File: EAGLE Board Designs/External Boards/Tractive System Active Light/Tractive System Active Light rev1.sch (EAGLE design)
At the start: 26 parts, among them X1 CONNECTOR-4NANO-FIT-VERTICAL-4

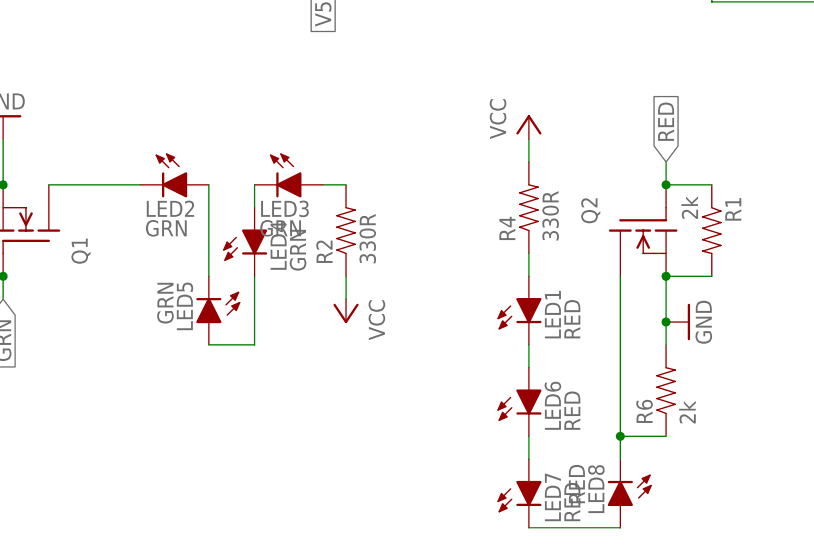
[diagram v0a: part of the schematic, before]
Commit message: Fixed thermal pads to have seperate net
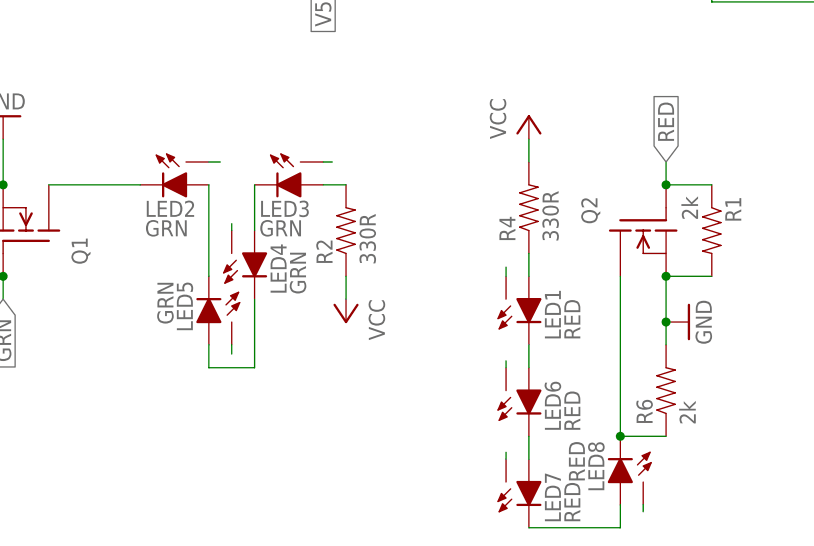
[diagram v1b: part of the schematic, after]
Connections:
- new net LED1_THERM: LED1.X
- new net LED2_THERM: LED2.X
- new net LED3_THERM: LED3.X
- new net LED4_THERM: LED4.X
- new net LED5_THERM: LED5.X
- new net LED6_THERM: LED6.X
- new net LED7_THERM: LED7.X
- new net LED8_THERM: LED8.X
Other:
- moved on the sheet: LED4, LED8
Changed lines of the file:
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@@
 <part name="Q1" library="HyTechDevices" deviceset="DMG3406L" device="SOT"/>
 <part name="Q2" library="HyTechDevices" deviceset="DMG3406L" device="SOT"/>
-<part name="NA555" library="HyTechDevices" deviceset="NA555" device="SO-8" package3d_urn="urn:adsk.eagle:package:30987/2"/>
+<part name="NA555" library="HyTechDevices" deviceset="NA555" device="SO-8"/>
 <part name="LED1" library="HyTechDevices" deviceset="XP-E2" device="XP-E2" value="RED"/>
 <part name="LED2" library="HyTechDevices" deviceset="XP-E2" device="XP-E2" value="GRN"/>
@@
 <attribute name="VALUE" x="3.048" y="32.385" size="1.778" layer="96"/>
 </instance>
-<instance part="LED4" gate="G$1" x="2.54" y="33.02" smashed="yes">
-<attribute name="NAME" x="6.096" y="28.448" size="1.778" layer="95" rot="R90"/>
-<attribute name="VALUE" x="8.255" y="28.448" size="1.778" layer="96" rot="R90"/>
+<instance part="LED4" gate="G$1" x="2.54" y="30.48" smashed="yes">
+<attribute name="NAME" x="6.096" y="25.908" size="1.778" layer="95" rot="R90"/>
+<attribute name="VALUE" x="8.255" y="25.908" size="1.778" layer="96" rot="R90"/>
 </instance>
 <instance part="LED5" gate="G$1" x="-2.54" y="22.86" smashed="yes" rot="R180">
@@
 <attribute name="VALUE" x="38.735" y="0.508" size="1.778" layer="96" rot="R90"/>
 </instance>
-<instance part="LED8" gate="G$1" x="43.18" y="2.54" smashed="yes" rot="R180">
-<attribute name="NAME" x="39.624" y="7.112" size="1.778" layer="95" rot="R270"/>
-<attribute name="VALUE" x="37.465" y="7.112" size="1.778" layer="96" rot="R270"/>
+<instance part="LED8" gate="G$1" x="43.18" y="5.08" smashed="yes" rot="R180">
+<attribute name="NAME" x="39.624" y="9.652" size="1.778" layer="95" rot="R270"/>
+<attribute name="VALUE" x="37.465" y="9.652" size="1.778" layer="96" rot="R270"/>
 </instance>
 <instance part="GND1" gate="1" x="-12.7" y="109.22" smashed="yes" rot="R90">
@@
 <wire x1="48.26" y1="10.16" x2="43.18" y2="10.16" width="0.1524" layer="91"/>
 <pinref part="LED8" gate="G$1" pin="C"/>
-<wire x1="43.18" y1="7.62" x2="43.18" y2="10.16" width="0.1524" layer="91"/>
 <junction x="43.18" y="10.16"/>
 </segment>
@@
 <pinref part="LED8" gate="G$1" pin="A"/>
 <wire x1="33.02" y1="0" x2="43.18" y2="0" width="0.1524" layer="91"/>
+<wire x1="43.18" y1="0" x2="43.18" y2="2.54" width="0.1524" layer="91"/>
 </segment>
 </net>
@@
 <segment>
 <pinref part="LED5" gate="G$1" pin="A"/>
-<wire x1="-2.54" y1="20.32" x2="2.54" y2="20.32" width="0.1524" layer="91"/>
-<wire x1="2.54" y1="20.32" x2="2.54" y2="27.94" width="0.1524" layer="91"/>
+<wire x1="-2.54" y1="20.32" x2="-2.54" y2="17.78" width="0.1524" layer="91"/>
+<wire x1="-2.54" y1="17.78" x2="2.54" y2="17.78" width="0.1524" layer="91"/>
+<wire x1="2.54" y1="17.78" x2="2.54" y2="25.4" width="0.1524" layer="91"/>
 <pinref part="LED4" gate="G$1" pin="C"/>
 </segment>
@@
 <segment>
 <pinref part="LED4" gate="G$1" pin="A"/>
-<wire x1="2.54" y1="35.56" x2="2.54" y2="38.1" width="0.1524" layer="91"/>
+<wire x1="2.54" y1="33.02" x2="2.54" y2="38.1" width="0.1524" layer="91"/>
 <pinref part="LED3" gate="G$1" pin="C"/>
 </segment>
@@
 <wire x1="53.34" y1="38.1" x2="48.26" y2="38.1" width="0.1524" layer="91"/>
 <junction x="48.26" y="38.1"/>
+</segment>
+</net>
+<net name="LED5_THERM" class="0">
+<segment>
+<pinref part="LED5" gate="G$1" pin="X"/>
+<wire x1="0" y1="19.304" x2="0" y2="20.32" width="0.1524" layer="91"/>
+</segment>
+</net>
+<net name="LED2_THERM" class="0">
+<segment>
+<pinref part="LED2" gate="G$1" pin="X"/>
+<wire x1="-2.54" y1="40.64" x2="-1.27" y2="40.64" width="0.1524" layer="91"/>
+</segment>
+</net>
+<net name="LED3_THERM" class="0">
+<segment>
+<pinref part="LED3" gate="G$1" pin="X"/>
+<wire x1="11.176" y1="40.64" x2="10.16" y2="40.64" width="0.1524" layer="91"/>
+</segment>
+</net>
+<net name="LED4_THERM" class="0">
+<segment>
+<pinref part="LED4" gate="G$1" pin="X"/>
+<wire x1="0" y1="33.02" x2="0" y2="33.782" width="0.1524" layer="91"/>
+</segment>
+</net>
+<net name="LED1_THERM" class="0">
+<segment>
+<pinref part="LED1" gate="G$1" pin="X"/>
+<wire x1="30.48" y1="27.94" x2="30.48" y2="28.956" width="0.1524" layer="91"/>
+</segment>
+</net>
+<net name="LED8_THERM" class="0">
+<segment>
+<pinref part="LED8" gate="G$1" pin="X"/>
+<wire x1="45.72" y1="2.54" x2="45.72" y2="1.778" width="0.1524" layer="91"/>
+</segment>
+</net>
+<net name="LED7_THERM" class="0">
+<segment>
+<pinref part="LED7" gate="G$1" pin="X"/>
+<wire x1="30.48" y1="7.62" x2="30.48" y2="8.382" width="0.1524" layer="91"/>
+</segment>
+</net>
+<net name="LED6_THERM" class="0">
+<segment>
+<pinref part="LED6" gate="G$1" pin="X"/>
+<wire x1="30.48" y1="17.78" x2="30.48" y2="18.542" width="0.1524" layer="91"/>
 </segment>
 </net>
@@
 will not be understood (or retained) with this version.
 </note>
-<note version="8.3" severity="warning">
-Since Version 8.3, EAGLE supports the association of 3D packages
-with devices in libraries, schematics, and board files. Those 3D
-packages will not be understood (or retained) with this version.
-</note>
 </compatibility>

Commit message: Added tolerances and voltage ratings
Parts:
- C1, C2, C3, C4, C5, C6: TOLERANCE (none) -> 5%; VOLTAGE (none) -> 25V
- R1, R2, R3, R4, R5, R6, R7: TOLERANCE (none) -> 1%
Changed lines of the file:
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@@
 <part name="LED1" library="HyTechDevices" deviceset="XP-E2" device="XP-E2" value="RED"/>
 <part name="LED2" library="HyTechDevices" deviceset="XP-E2" device="XP-E2" value="GRN"/>
-<part name="R3" library="HyTechDevices" deviceset="RESISTOR" device="0603-RES" value="50k"/>
-<part name="R4" library="HyTechDevices" deviceset="RESISTOR" device="0603-RES" value="330R"/>
-<part name="R5" library="HyTechDevices" deviceset="RESISTOR" device="0603-RES" value="1k"/>
-<part name="C1" library="HyTechDevices" deviceset="CAP" device="0603-CAP" value="4.7uF"/>
+<part name="R3" library="HyTechDevices" deviceset="RESISTOR" device="0603-RES" value="50k">
+<attribute name="TOLERANCE" value="1%"/>
+</part>
+<part name="R4" library="HyTechDevices" deviceset="RESISTOR" device="0603-RES" value="330R">
+<attribute name="TOLERANCE" value="1%"/>
+</part>
+<part name="R5" library="HyTechDevices" deviceset="RESISTOR" device="0603-RES" value="1k">
+<attribute name="TOLERANCE" value="1%"/>
+</part>
+<part name="C1" library="HyTechDevices" deviceset="CAP" device="0603-CAP" value="4.7uF">
+<attribute name="TOLERANCE" value="5%"/>
+<attribute name="VOLTAGE" value="25V"/>
+</part>
 <part name="X1" library="HyTechDevices" deviceset="CONNECTOR-4" device="NANO-FIT-VERTICAL-4"/>
-<part name="C2" library="HyTechDevices" deviceset="CAP" device="0603-CAP" value="10nF"/>
-<part name="R6" library="HyTechDevices" deviceset="RESISTOR" device="0603-RES" value="2k"/>
-<part name="R2" library="HyTechDevices" deviceset="RESISTOR" device="0603-RES" value="330R"/>
+<part name="C2" library="HyTechDevices" deviceset="CAP" device="0603-CAP" value="10nF">
+<attribute name="TOLERANCE" value="5%"/>
+<attribute name="VOLTAGE" value="25V"/>
+</part>
+<part name="R6" library="HyTechDevices" deviceset="RESISTOR" device="0603-RES" value="2k">
+<attribute name="TOLERANCE" value="1%"/>
+</part>
+<part name="R2" library="HyTechDevices" deviceset="RESISTOR" device="0603-RES" value="330R">
+<attribute name="TOLERANCE" value="1%"/>
+</part>
 <part name="LED3" library="HyTechDevices" deviceset="XP-E2" device="XP-E2" value="GRN"/>
 <part name="LED4" library="HyTechDevices" deviceset="XP-E2" device="XP-E2" value="GRN"/>
@@
 <part name="P+2" library="supply1" library_urn="urn:adsk.eagle:library:371" deviceset="VCC" device=""/>
 <part name="P+4" library="supply1" library_urn="urn:adsk.eagle:library:371" deviceset="VCC" device=""/>
-<part name="C3" library="HyTechDevices" deviceset="CAP" device="0603-CAP" value="0.1uF"/>
-<part name="C4" library="HyTechDevices" deviceset="CAP" device="0603-CAP" value="1uF"/>
-<part name="C5" library="HyTechDevices" deviceset="CAP" device="0603-CAP" value="1uF"/>
-<part name="C6" library="HyTechDevices" deviceset="CAP" device="0603-CAP" value="0.1uF"/>
+<part name="C3" library="HyTechDevices" deviceset="CAP" device="0603-CAP" value="0.1uF">
+<attribute name="TOLERANCE" value="5%"/>
+<attribute name="VOLTAGE" value="25V"/>
+</part>
+<part name="C4" library="HyTechDevices" deviceset="CAP" device="0603-CAP" value="1uF">
+<attribute name="TOLERANCE" value="5%"/>
+<attribute name="VOLTAGE" value="25V"/>
+</part>
+<part name="C5" library="HyTechDevices" deviceset="CAP" device="0603-CAP" value="1uF">
+<attribute name="TOLERANCE" value="5%"/>
+<attribute name="VOLTAGE" value="25V"/>
+</part>
+<part name="C6" library="HyTechDevices" deviceset="CAP" device="0603-CAP" value="0.1uF">
+<attribute name="TOLERANCE" value="5%"/>
+<attribute name="VOLTAGE" value="25V"/>
+</part>
 <part name="GND6" library="HyTechSymbols" deviceset="GND" device=""/>
 <part name="P+5" library="supply1" library_urn="urn:adsk.eagle:library:371" deviceset="VCC" device=""/>
@@
 <part name="P+3" library="supply1" library_urn="urn:adsk.eagle:library:371" deviceset="VCC" device=""/>
 <part name="GND3" library="HyTechSymbols" deviceset="GND" device=""/>
-<part name="R7" library="HyTechDevices" deviceset="RESISTOR" device="0603-RES" value="2k"/>
-<part name="R1" library="HyTechDevices" deviceset="RESISTOR" device="0603-RES" value="2k"/>
+<part name="R7" library="HyTechDevices" deviceset="RESISTOR" device="0603-RES" value="2k">
+<attribute name="TOLERANCE" value="1%"/>
+</part>
+<part name="R1" library="HyTechDevices" deviceset="RESISTOR" device="0603-RES" value="2k">
+<attribute name="TOLERANCE" value="1%"/>
+</part>
 </parts>
 <sheets>
@@
 <attribute name="NAME" x="51.8414" y="77.47" size="1.778" layer="95" rot="R90"/>
 <attribute name="VALUE" x="56.642" y="77.47" size="1.778" layer="96" rot="R90"/>
+<attribute name="TOLERANCE" x="53.34" y="81.28" size="0.127" layer="96" rot="R90" display="off"/>
 </instance>
 <instance part="R4" gate="G$1" x="33.02" y="35.56" smashed="yes" rot="R90">
 <attribute name="NAME" x="31.5214" y="31.75" size="1.778" layer="95" rot="R90"/>
 <attribute name="VALUE" x="36.322" y="31.75" size="1.778" layer="96" rot="R90"/>
+<attribute name="TOLERANCE" x="33.02" y="35.56" size="0.127" layer="96" rot="R90" display="off"/>
 </instance>
 <instance part="R5" gate="G$1" x="53.34" y="93.98" smashed="yes" rot="R270">
 <attribute name="NAME" x="54.8386" y="97.79" size="1.778" layer="95" rot="R270"/>
 <attribute name="VALUE" x="50.038" y="97.79" size="1.778" layer="96" rot="R270"/>
+<attribute name="TOLERANCE" x="53.34" y="93.98" size="0.127" layer="96" rot="R270" display="off"/>
 </instance>
 <instance part="C1" gate="G$1" x="76.2" y="58.42" smashed="yes" rot="R90">
 <attribute name="NAME" x="73.279" y="59.944" size="1.778" layer="95" rot="R90"/>
 <attribute name="VALUE" x="78.359" y="59.944" size="1.778" layer="96" rot="R90"/>
+<attribute name="TOLERANCE" x="76.2" y="58.42" size="0.127" layer="96" rot="R90" display="off"/>
+<attribute name="VOLTAGE" x="76.2" y="58.42" size="0.127" layer="96" rot="R90" display="off"/>
 </instance>
 <instance part="X1" gate="-1" x="-20.32" y="109.22" smashed="yes" rot="MR0">
@@
 <attribute name="NAME" x="98.044" y="68.961" size="1.778" layer="95"/>
 <attribute name="VALUE" x="98.044" y="63.881" size="1.778" layer="96"/>
+<attribute name="TOLERANCE" x="96.52" y="66.04" size="0.127" layer="96" display="off"/>
+<attribute name="VOLTAGE" x="96.52" y="66.04" size="0.127" layer="96" display="off"/>
 </instance>
 <instance part="R6" gate="G$1" x="48.26" y="15.24" smashed="yes" rot="R90">
 <attribute name="NAME" x="46.7614" y="11.43" size="1.778" layer="95" rot="R90"/>
 <attribute name="VALUE" x="51.562" y="11.43" size="1.778" layer="96" rot="R90"/>
+<attribute name="TOLERANCE" x="48.26" y="15.24" size="0.127" layer="96" rot="R90" display="off"/>
 </instance>
 <instance part="R2" gate="G$1" x="12.7" y="33.02" smashed="yes" rot="R90">
 <attribute name="NAME" x="11.2014" y="29.21" size="1.778" layer="95" rot="R90"/>
 <attribute name="VALUE" x="16.002" y="29.21" size="1.778" layer="96" rot="R90"/>
+<attribute name="TOLERANCE" x="12.7" y="33.02" size="0.127" layer="96" rot="R90" display="off"/>
 </instance>
 <instance part="LED3" gate="G$1" x="7.62" y="38.1" smashed="yes" rot="R270">
@@
 <attribute name="NAME" x="80.899" y="24.384" size="1.778" layer="95" rot="R90"/>
 <attribute name="VALUE" x="85.979" y="24.384" size="1.778" layer="96" rot="R90"/>
+<attribute name="TOLERANCE" x="83.82" y="22.86" size="0.127" layer="96" rot="R90" display="off"/>
+<attribute name="VOLTAGE" x="83.82" y="22.86" size="0.127" layer="96" rot="R90" display="off"/>
 </instance>
 <instance part="C4" gate="G$1" x="83.82" y="15.24" smashed="yes" rot="R90">
 <attribute name="NAME" x="80.899" y="16.764" size="1.778" layer="95" rot="R90"/>
 <attribute name="VALUE" x="85.979" y="16.764" size="1.778" layer="96" rot="R90"/>
+<attribute name="TOLERANCE" x="83.82" y="15.24" size="0.127" layer="96" rot="R90" display="off"/>
+<attribute name="VOLTAGE" x="83.82" y="15.24" size="0.127" layer="96" rot="R90" display="off"/>
 </instance>
 <instance part="C5" gate="G$1" x="25.4" y="104.14" smashed="yes" rot="R270">
 <attribute name="NAME" x="28.321" y="102.616" size="1.778" layer="95" rot="R270"/>
 <attribute name="VALUE" x="23.241" y="102.616" size="1.778" layer="96" rot="R270"/>
+<attribute name="TOLERANCE" x="25.4" y="104.14" size="0.127" layer="96" rot="R270" display="off"/>
+<attribute name="VOLTAGE" x="25.4" y="104.14" size="0.127" layer="96" rot="R270" display="off"/>
 </instance>
 <instance part="C6" gate="G$1" x="25.4" y="96.52" smashed="yes" rot="R270">
 <attribute name="NAME" x="28.321" y="94.996" size="1.778" layer="95" rot="R270"/>
 <attribute name="VALUE" x="23.241" y="94.996" size="1.778" layer="96" rot="R270"/>
+<attribute name="TOLERANCE" x="25.4" y="96.52" size="0.127" layer="96" rot="R270" display="off"/>
+<attribute name="VOLTAGE" x="25.4" y="96.52" size="0.127" layer="96" rot="R270" display="off"/>
 </instance>
 <instance part="GND6" gate="1" x="86.36" y="35.56" smashed="yes" rot="R180">
@@
 <attribute name="NAME" x="-31.9786" y="29.21" size="1.778" layer="95" rot="R90"/>
 <attribute name="VALUE" x="-27.178" y="29.21" size="1.778" layer="96" rot="R90"/>
+<attribute name="TOLERANCE" x="-30.48" y="33.02" size="0.127" layer="96" rot="R90" display="off"/>
 </instance>
 <instance part="R1" gate="G$1" x="53.34" y="33.02" smashed="yes" rot="R270">
 <attribute name="NAME" x="54.8386" y="36.83" size="1.778" layer="95" rot="R270"/>
 <attribute name="VALUE" x="50.038" y="36.83" size="1.778" layer="96" rot="R270"/>
+<attribute name="TOLERANCE" x="53.34" y="33.02" size="0.127" layer="96" rot="R270" display="off"/>
 </instance>
 </instances>
